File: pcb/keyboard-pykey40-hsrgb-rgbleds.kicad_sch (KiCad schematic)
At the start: 107 parts, among them Q1 Q_NMOS_GSD

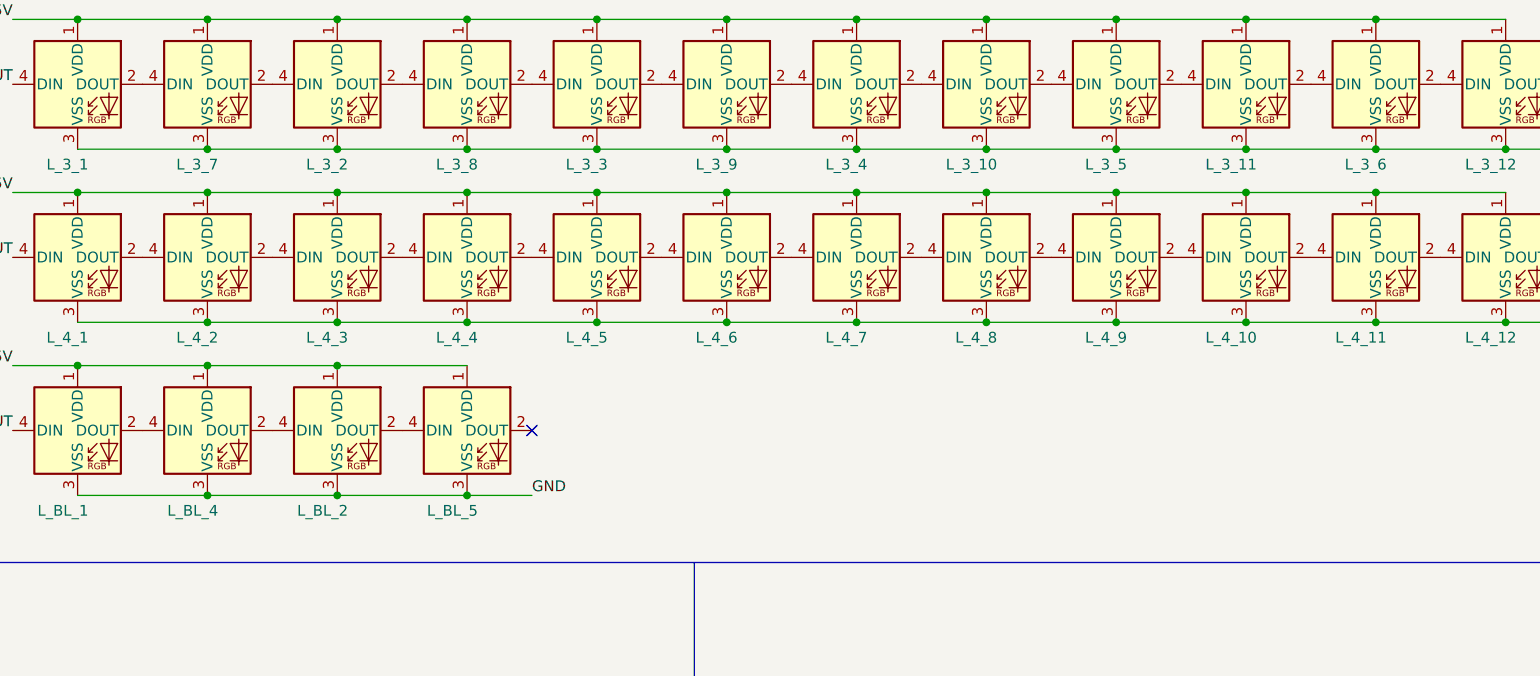
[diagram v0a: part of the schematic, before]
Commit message: pcb: save keyboard-pykey40-hsrgb with kicad9
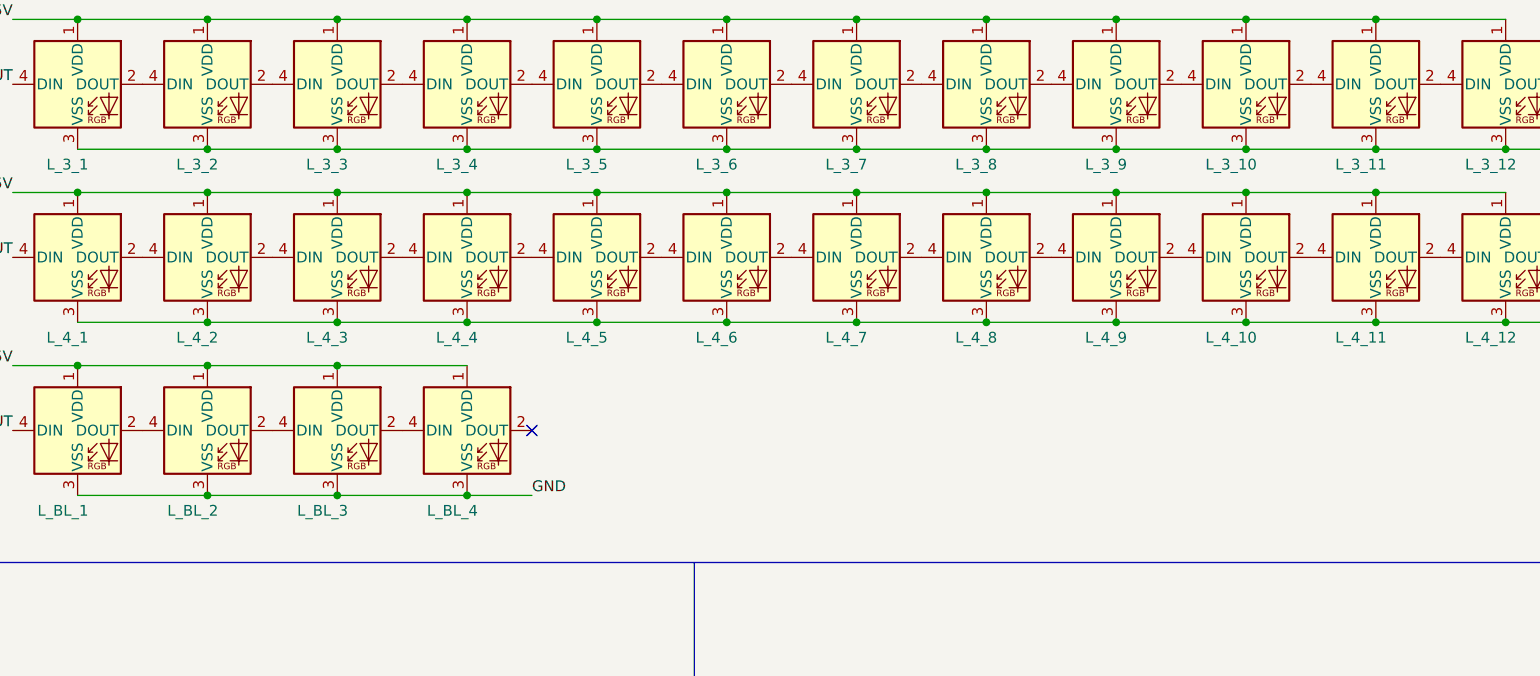
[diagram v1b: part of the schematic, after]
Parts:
- renumbered L_3_11 to L_3_10, L_3_6 to L_3_11, L_3_7 to L_3_2, L_3_2 to L_3_3, L_3_8 to L_3_4, L_3_3 to L_3_5, L_3_9 to L_3_6, L_3_4 to L_3_7, L_3_10 to L_3_8, L_3_5 to L_3_9, L_BL_4 to L_BL_2, L_BL_2 to L_BL_3, L_BL_5 to L_BL_4
